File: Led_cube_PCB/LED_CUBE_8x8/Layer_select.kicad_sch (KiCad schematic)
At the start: 4 parts, among them IC31 SN74HCS238DYYR, IC32 TBD62083AFNG,EL, J9 Conn_02x04_Top_Bottom

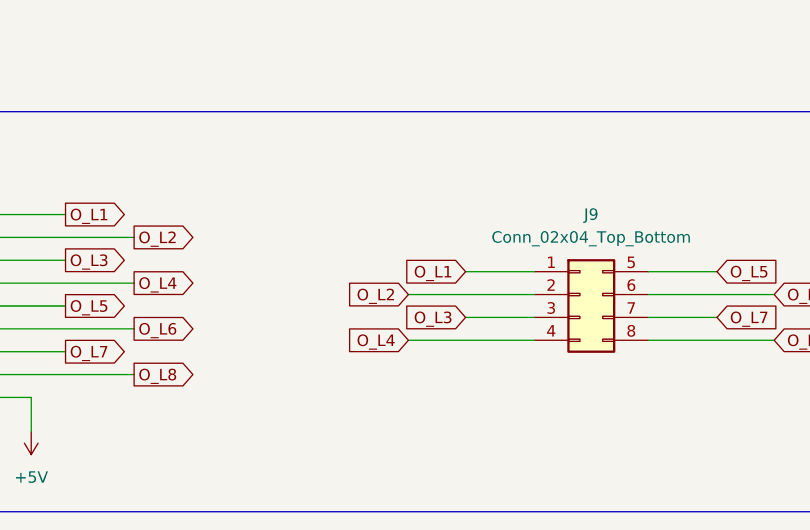
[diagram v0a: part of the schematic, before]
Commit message: Added test points and solder jumpers
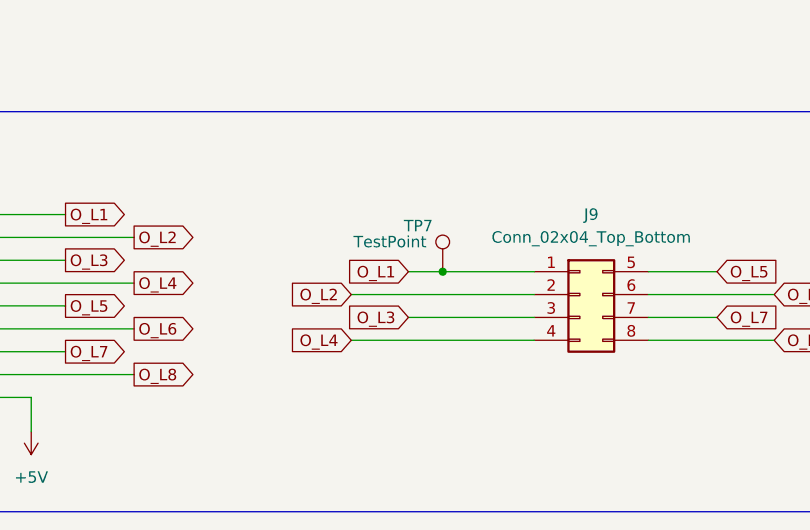
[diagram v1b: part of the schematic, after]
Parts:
- added TP7: TestPoint, TestPoint:TestPoint_Pad_D2.0mm, symbol Connector:TestPoint
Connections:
- net O_L1: now also TP7.1
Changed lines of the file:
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@@
+	)
+	(junction
+		(at 140.97 88.9)
+		(diameter 0)
+		(color 0 0 0 0)
 	)
 	(junction
@@
 	(wire
 		(pts
-			(xy 143.51 93.98) (xy 151.13 93.98)
+			(xy 137.16 93.98) (xy 151.13 93.98)
 		)
 		(stroke
@@
 	(wire
 		(pts
-			(xy 137.16 96.52) (xy 151.13 96.52)
+			(xy 130.81 96.52) (xy 151.13 96.52)
 		)
 		(stroke
@@
 	(wire
 		(pts
-			(xy 143.51 88.9) (xy 151.13 88.9)
-		)
-		(stroke
-			(width 0)
-			(type default)
-		)
-	)
-	(wire
-		(pts
-			(xy 137.16 91.44) (xy 151.13 91.44)
+			(xy 137.16 88.9) (xy 140.97 88.9)
+		)
+		(stroke
+			(width 0)
+			(type default)
+		)
+	)
+	(wire
+		(pts
+			(xy 140.97 88.9) (xy 151.13 88.9)
+		)
+		(stroke
+			(width 0)
+			(type default)
+		)
+	)
+	(wire
+		(pts
+			(xy 130.81 91.44) (xy 151.13 91.44)
 		)
 		(stroke
@@
 	(global_label "O_L1"
 		(shape input)
-		(at 143.51 88.9 180)
+		(at 137.16 88.9 180)
 		(fields_autoplaced yes)
 		(effects
@@
 		)
 		(property "Intersheetrefs" "${INTERSHEET_REFS}"
-			(at 135.9891 88.9 0)
+			(at 129.6391 88.9 0)
 			(hide yes)
 			(show_name no)
@@
 	(global_label "O_L4"
 		(shape input)
-		(at 137.16 96.52 180)
+		(at 130.81 96.52 180)
 		(fields_autoplaced yes)
 		(effects
@@
 		)
 		(property "Intersheetrefs" "${INTERSHEET_REFS}"
-			(at 129.6391 96.52 0)
+			(at 123.2891 96.52 0)
 			(hide yes)
 			(show_name no)
@@
 	(global_label "O_L2"
 		(shape input)
-		(at 137.16 91.44 180)
+		(at 130.81 91.44 180)
 		(fields_autoplaced yes)
 		(effects
@@
 		)
 		(property "Intersheetrefs" "${INTERSHEET_REFS}"
-			(at 129.6391 91.44 0)
+			(at 123.2891 91.44 0)
 			(hide yes)
 			(show_name no)
@@
 	(global_label "O_L3"
 		(shape input)
-		(at 143.51 93.98 180)
+		(at 137.16 93.98 180)
 		(fields_autoplaced yes)
 		(effects
@@
 		)
 		(property "Intersheetrefs" "${INTERSHEET_REFS}"
-			(at 135.9891 93.98 0)
+			(at 129.6391 93.98 0)
 			(hide yes)
 			(show_name no)
@@
 					(unit 1)
 				)
+			)
+		)
+	)
+	(symbol
+		(lib_id "Connector:TestPoint")
+		(at 140.97 88.9 0)
+		(unit 1)
+		(body_style 1)
+		(exclude_from_sim no)
+		(in_bom yes)
+		(on_board yes)
+		(in_pos_files yes)
+		(dnp no)
+		(property "Reference" "TP7"
+			(at 136.652 83.82 0)
+			(show_name no)
+			(do_not_autoplace no)
+			(effects
+				(font
+					(size 1.27 1.27)
+				)
+				(justify left)
+			)
+		)
+		(property "Value" "TestPoint"
+			(at 131.064 85.598 0)
+			(show_name no)
+			(do_not_autoplace no)
+			(effects
+				(font
+					(size 1.27 1.27)
+				)
+				(justify left)
+			)
+		)
+		(property "Footprint" "TestPoint:TestPoint_Pad_D2.0mm"
+			(at 146.05 88.9 0)
+			(hide yes)
+			(show_name no)
+			(do_not_autoplace no)
+			(effects
+				(font
+					(size 1.27 1.27)
+				)
+			)
+		)
+		(property "Datasheet" ""
+			(at 146.05 88.9 0)
+			(hide yes)
+			(show_name no)
+			(do_not_autoplace no)
+			(effects
+				(font
+					(size 1.27 1.27)
+				)
+			)
+		)
+		(property "Description" "test point"
+			(at 140.97 88.9 0)
+			(hide yes)
+			(show_name no)
+			(do_not_autoplace no)
+			(effects
+				(font
+					(size 1.27 1.27)
+				)
+			)
+		)
+		(pin "1"
+		)
+		(instances
+			(project "LED_CUBE_8x8"
+				(path "/b239677e-e361-4439-8200-63fb41f7e03c/905dac8e-5dc9-4853-8a58-87c51247ef9b"
+					(reference "TP7")
+					(unit 1)
+				)
